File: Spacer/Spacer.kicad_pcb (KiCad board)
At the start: 2 copper layers, 35.4 x 24.6 mm, 4 parts, among them J1 IN, J2 OUT, J3 nOEInject

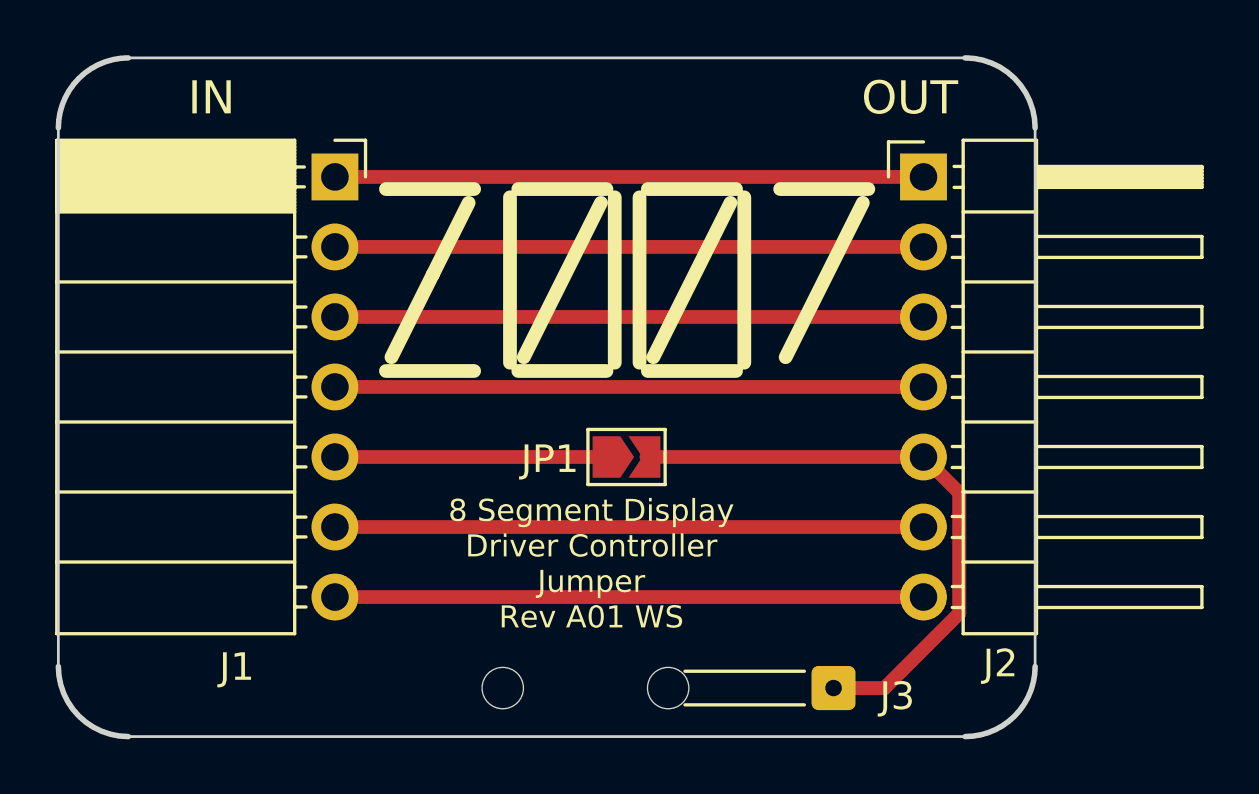
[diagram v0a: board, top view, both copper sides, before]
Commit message: updated silk
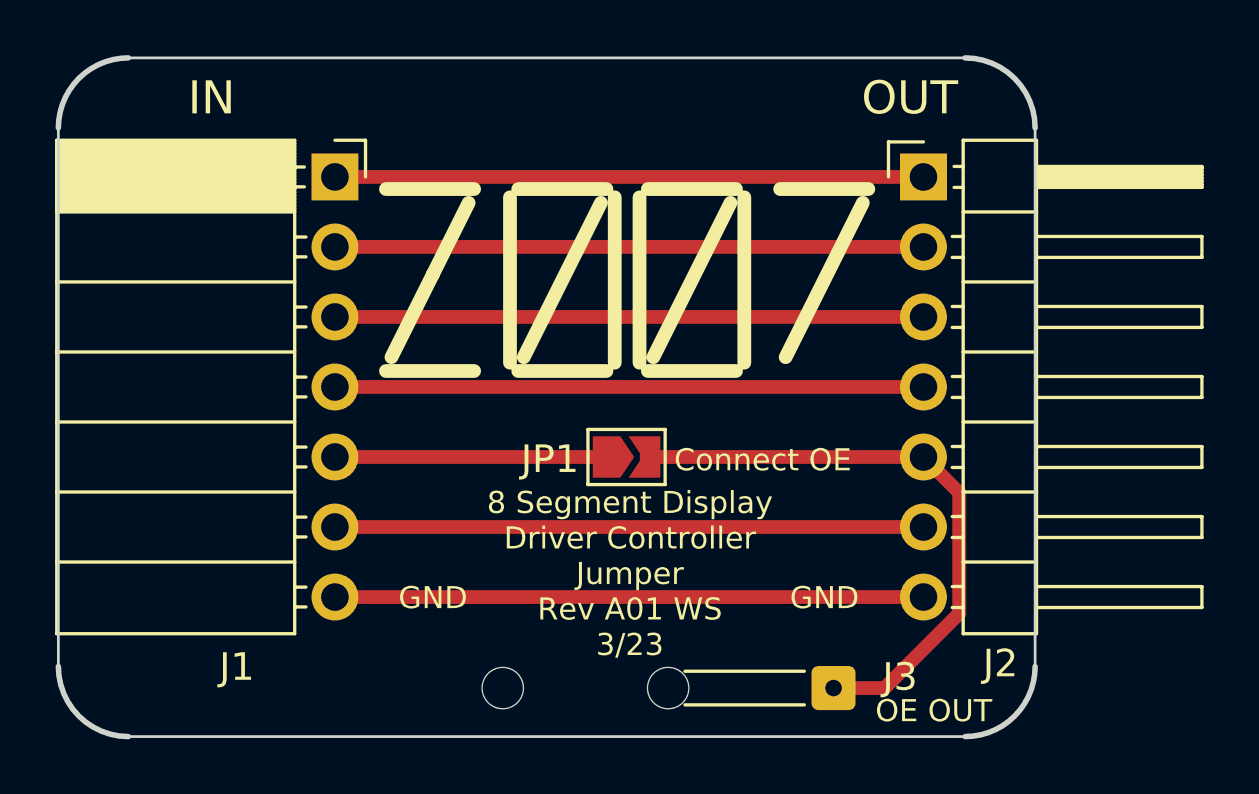
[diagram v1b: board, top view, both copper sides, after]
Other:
- board text added: "8 Segment Display Driver Controller Jumper Rev A01 WS 3/23"
- board text added: "Connect OE"
- board text added: "GND"
- board text added: "OE OUT"
- board text removed: "8 Segment Display Driver Controller Jumper Rev A01 WS"
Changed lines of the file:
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@@
     (property "ki_keywords" "connector")
     (attr exclude_from_pos_files)
-    (fp_text reference "J3" (at 0.298 -2.312) (layer "F.SilkS")
+    (fp_text reference "J3" (at -0.402 -2.412) (layer "F.SilkS")
         (effects (font (size 1 1) (thickness 0.15)))
     )
@@
   (gr_arc (start 110.617 64.262) (mid 111.360948 62.465948) (end 113.157 61.722)
     (stroke (width 0.2) (type default)) (layer "Edge.Cuts"))
+  (gr_text "GND" (at 125.55 81.78) (layer "B.SilkS" knockout)
+    (effects (font (size 0.8 0.8) (thickness 0.12)) (justify left bottom mirror))
+  )
   (gr_text "OUT\n" (at 143.35 63.88) (layer "B.SilkS" knockout)
     (effects (font (size 1.2 1.2) (thickness 0.12)) (justify left bottom mirror))
   )
+  (gr_text "OE OUT" (at 144.35 85.78) (layer "B.SilkS")
+    (effects (font (size 0.8 0.8) (thickness 0.12)) (justify left bottom mirror))
+  )
+  (gr_text "GND" (at 139.75 81.78) (layer "B.SilkS" knockout)
+    (effects (font (size 0.8 0.8) (thickness 0.12)) (justify left bottom mirror))
+  )
   (gr_text "IN" (at 117.15 63.88) (layer "B.SilkS" knockout)
     (effects (font (size 1.2 1.2) (thickness 0.12)) (justify left bottom mirror))
@@
     (effects (font (size 1.2 1.2) (thickness 0.12)) (justify left bottom))
   )
-  (gr_text "8 Segment Display\nDriver Controller \nJumper\nRev A01 WS" (at 129.95 82.48) (layer "F.SilkS")
+  (gr_text "GND" (at 137.15 81.78) (layer "F.SilkS" knockout)
+    (effects (font (size 0.8 0.8) (thickness 0.12)) (justify left bottom))
+  )
+  (gr_text "Connect OE" (at 132.95 76.78) (layer "F.SilkS")
+    (effects (font (size 0.8 0.8) (thickness 0.12)) (justify left bottom))
+  )
+  (gr_text "OE OUT" (at 140.25 85.88) (layer "F.SilkS")
+    (effects (font (size 0.8 0.8) (thickness 0.12)) (justify left bottom))
+  )
+  (gr_text "8 Segment Display\nDriver Controller \nJumper\nRev A01 WS\n3/23" (at 131.35 83.48) (layer "F.SilkS")
     (effects (font (size 0.8 0.8) (thickness 0.12)) (justify bottom))
   )
+  (gr_text "GND" (at 122.95 81.78) (layer "F.SilkS" knockout)
+    (effects (font (size 0.8 0.8) (thickness 0.12)) (justify left bottom))
+  )
   (segment (start 142 66.04) (end 120.65 66.04) (width 0.5) (layer "F.Cu") (net 1))
